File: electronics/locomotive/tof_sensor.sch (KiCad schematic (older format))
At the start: 0 parts

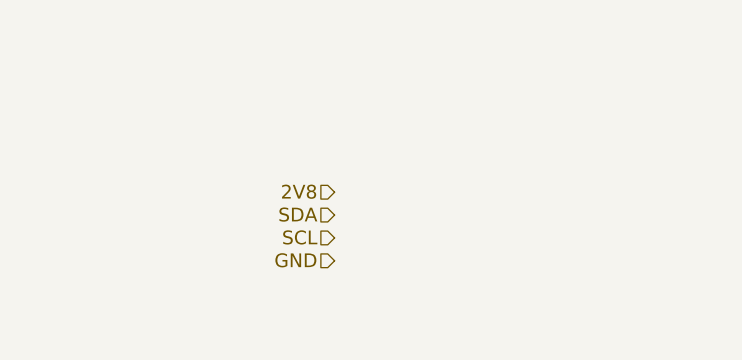
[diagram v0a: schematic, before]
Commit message: electronics: locomotive: Update schematics
Voltage regulator, TOF, IR receiver, voltage scaler, I2C control lines, power
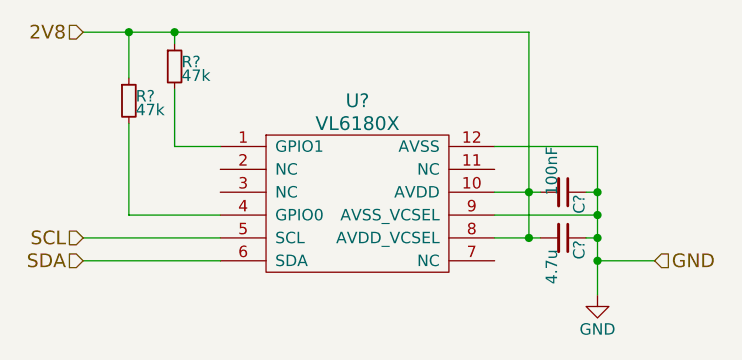
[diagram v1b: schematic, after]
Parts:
- added C?: 100nF, symbol C_Small
- added C?: 4.7u, symbol C_Small
- added R? (x2): 47k, symbol R_Small
- added U?: VL6180X, symbol VL6180X
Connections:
- net 2V8: now also C?.2, C?.2, R?.1, R?.1, U?.10 (AVDD~), U?.8 (AVDD_VCSEL)
- net GND: now also C?.1, C?.1, U?.12 (AVSS), U?.9 (AVSS_VCSEL)
- net SCL: now also U?.5 (SCL)
- net SDA: now also U?.6 (SDA)
- new net: R?.2, U?.1 (GPIO1)
- new net: R?.2, U?.4 (GPIO0)
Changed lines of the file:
@@
 LIBS:valves
 LIBS:stm32
+LIBS:SPX3819
 LIBS:bcan
+LIBS:TSOP57238
 LIBS:locomotive-cache
 EELAYER 25 0
@@
 Comment4 ""
 $EndDescr
-Text HLabel 5700 4200 0    60   Input ~ 0
+Text HLabel 4600 4400 0    60   Input ~ 0
 SDA
-Text HLabel 5700 4300 0    60   Input ~ 0
+Text HLabel 4600 4300 0    60   Input ~ 0
 SCL
-Text HLabel 5700 4100 0    60   Input ~ 0
+Text HLabel 4600 3400 0    60   Input ~ 0
 2V8
-Text HLabel 5700 4400 0    60   Input ~ 0
+Text HLabel 7100 4400 2    60   Input ~ 0
 GND
+$Comp
+L VL6180X U?
+U 1 1 58C369EE
+P 5750 3700
+F 0 "U?" H 5800 3700 60  0000 C CNN
+F 1 "VL6180X" H 5800 3600 60  0000 C CNN
+F 2 "" H 5800 3700 60  0001 C CNN
+F 3 "" H 5800 3700 60  0001 C CNN
+	1    5750 3700
+	1    0    0    -1
+$EndComp
+$Comp
+L R_Small R?
+U 1 1 58C370B7
+P 4800 3700
+F 0 "R?" H 4830 3720 50  0000 L CNN
+F 1 "47k" H 4830 3660 50  0000 L CNN
+F 2 "" H 4800 3700 50  0001 C CNN
+F 3 "" H 4800 3700 50  0001 C CNN
+	1    4800 3700
+	1    0    0    -1
+$EndComp
+$Comp
+L R_Small R?
+U 1 1 58C370BD
+P 5000 3550
+F 0 "R?" H 5030 3570 50  0000 L CNN
+F 1 "47k" H 5030 3510 50  0000 L CNN
+F 2 "" H 5000 3550 50  0001 C CNN
+F 3 "" H 5000 3550 50  0001 C CNN
+	1    5000 3550
+	1    0    0    -1
+$EndComp
+Wire Wire Line
+	4800 3400 4800 3600
+Wire Wire Line
+	4800 3800 4800 4200
+Wire Wire Line
+	4800 4200 5200 4200
+Wire Wire Line
+	5000 3650 5000 3900
+Wire Wire Line
+	5000 3900 5200 3900
+Wire Wire Line
+	6550 3400 6550 4300
+Wire Wire Line
+	6400 4100 6600 4100
+Wire Wire Line
+	6400 4300 6600 4300
+Connection ~ 6550 4100
+$Comp
+L GND #PWR040
+U 1 1 58C379FA
+P 6850 4550
+F 0 "#PWR040" H 6850 4300 50  0001 C CNN
+F 1 "GND" H 6850 4400 50  0000 C CNN
+F 2 "" H 6850 4550 50  0001 C CNN
+F 3 "" H 6850 4550 50  0001 C CNN
+	1    6850 4550
+	1    0    0    -1
+$EndComp
+Wire Wire Line
+	6400 3900 6850 3900
+Wire Wire Line
+	6850 3900 6850 4550
+Wire Wire Line
+	6850 4400 7100 4400
+Connection ~ 6850 4400
+Wire Wire Line
+	6400 4200 6850 4200
+Connection ~ 6850 4200
+$Comp
+L C_Small C?
+U 1 1 58C37BD2
+P 6700 4100
+F 0 "C?" H 6710 4170 50  0000 L CNN
+F 1 "100nF" H 6500 4050 50  0000 L CNN
+F 2 "" H 6700 4100 50  0001 C CNN
+F 3 "" H 6700 4100 50  0001 C CNN
+	1    6700 4100
+	0    1    1    0
+$EndComp
+$Comp
+L C_Small C?
+U 1 1 58C37C29
+P 6700 4300
+F 0 "C?" H 6710 4370 50  0000 L CNN
+F 1 "4.7u" H 6750 4250 50  0000 L CNN
+F 2 "" H 6700 4300 50  0001 C CNN
+F 3 "" H 6700 4300 50  0001 C CNN
+	1    6700 4300
+	0    1    1    0
+$EndComp
+Wire Wire Line
+	6800 4100 6850 4100
+Connection ~ 6850 4100
+Connection ~ 6550 4300
+Wire Wire Line
+	6800 4300 6850 4300
+Connection ~ 6850 4300
+Wire Wire Line
+	4600 3400 6550 3400
+Wire Wire Line
+	5000 3450 5000 3400
+Connection ~ 5000 3400
+Connection ~ 4800 3400
+Wire Wire Line
+	4600 4300 5200 4300
+Wire Wire Line
+	4600 4400 5200 4400
 $EndSCHEMATC
